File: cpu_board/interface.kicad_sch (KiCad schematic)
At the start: 10 parts, among them J5 Conn_01x06, J8 Conn_01x02

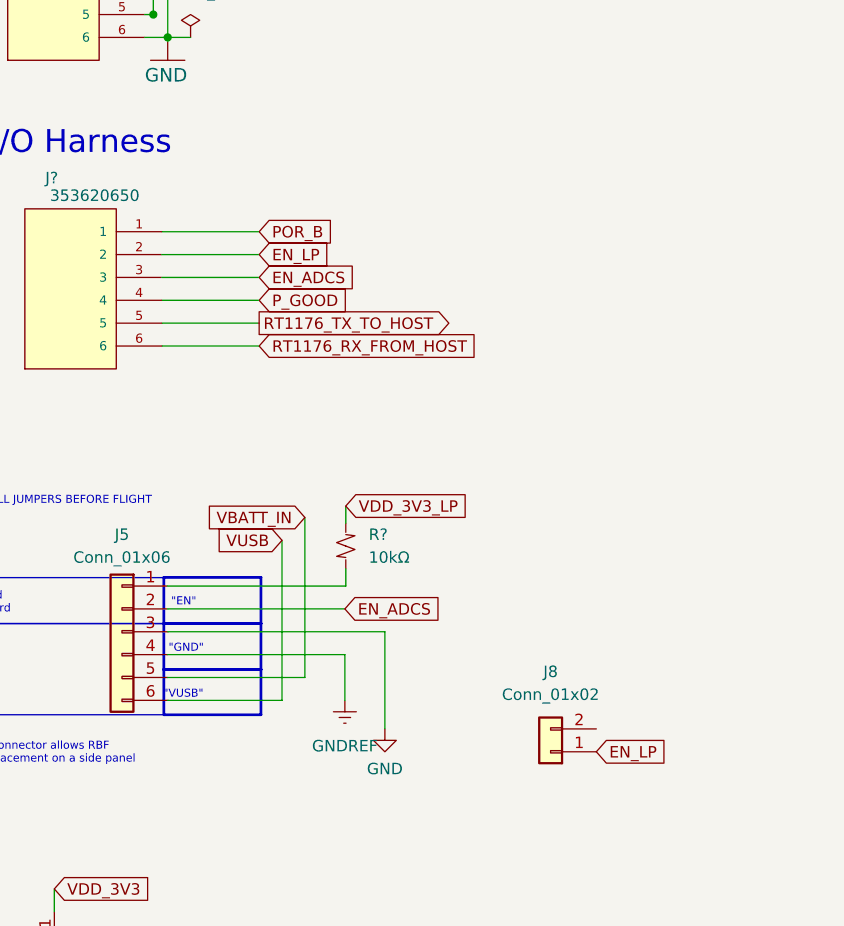
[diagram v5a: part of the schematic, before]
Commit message: move level shifter to top
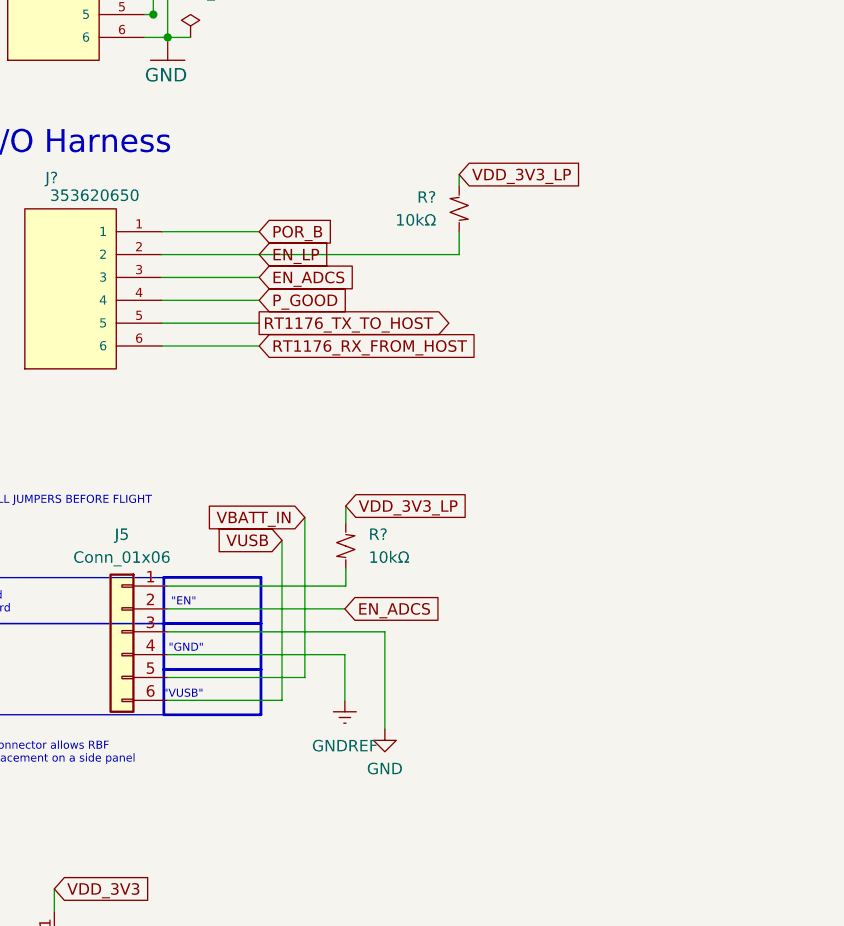
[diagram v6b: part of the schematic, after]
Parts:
- removed J8: Conn_01x02, symbol Connector_Generic:Conn_01x02
- added R?: 10kΩ, adcs:Perfect_0402, symbol Device:R_Small_US
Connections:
- net EN_LP: now also R?.2
- net VDD_3V3_LP: now also R?.1
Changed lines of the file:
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@@
   (junction (at 198.755 93.345) (diameter 0) (color 0 0 0 0)
   )
+  (wire (pts (xy 231.14 117.475) (xy 198.12 117.475))
+    (stroke (width 0) (type default))
+  )
   (wire (pts (xy 198.755 93.345) (xy 196.215 93.345))
     (stroke (width 0) (type default))
@@
     (stroke (width 0) (type default))
   )
+  (wire (pts (xy 231.14 114.935) (xy 231.14 117.475))
+    (stroke (width 0) (type default))
+  )
   (wire (pts (xy 198.12 125.095) (xy 208.915 125.095))
     (stroke (width 0) (type default))
   )
-  (wire (pts (xy 198.12 117.475) (xy 208.915 117.475))
-    (stroke (width 0) (type default))
-  )
   (wire (pts (xy 198.755 159.385) (xy 222.885 159.385))
     (stroke (width 0) (type default))
@@
   )
   (wire (pts (xy 197.1548 90.8304) (xy 197.1548 90.805))
+    (stroke (width 0) (type default))
+  )
+  (wire (pts (xy 231.14 108.585) (xy 231.14 109.855))
     (stroke (width 0) (type default))
   )
@@
   (text "Mounting Holes" (at 300.99 182.88 0)
     (effects (font (size 2.159 2.159)) (justify left bottom))
+  )
+  (global_label "VDD_3V3_LP" (shape input) (at 231.14 108.585 0) (fields_autoplaced)
+    (effects (font (size 1.27 1.27)) (justify left))
+    (property "Intersheetrefs" "${INTERSHEET_REFS}" (at 245.4947 108.585 0)
+      (effects (font (size 1.27 1.27)) (justify left) hide)
+    )
   )
   (global_label "VBATT_IN" (shape input) (at 198.755 80.645 0) (fields_autoplaced)
@@
     (property "Intersheetrefs" "${INTERSHEET_REFS}" (at 202.7245 146.685 0)
       (effects (font (size 1.27 1.27)) (justify right) hide)
-    )
-  )
-  (global_label "EN_LP" (shape input) (at 246.38 172.72 0) (fields_autoplaced)
-    (effects (font (size 1.27 1.27)) (justify left))
-    (property "Intersheetrefs" "${INTERSHEET_REFS}" (at 255.1104 172.72 0)
-      (effects (font (size 1.27 1.27)) (justify left) hide)
     )
   )
@@
         (path "/db20b18b-d25a-428e-8229-70a189e1de75/00000000-0000-0000-0000-00005cec60eb"
           (reference "J?") (unit 1)
-        )
-      )
-    )
-  )
-  (symbol (lib_id "Connector_Generic:Conn_01x02") (at 241.3 172.72 180) (unit 1)
-    (in_bom yes) (on_board yes) (dnp no) (fields_autoplaced)
-    (property "Reference" "J8" (at 241.3 163.83 0)
-      (effects (font (size 1.27 1.27)))
-    )
-    (property "Value" "Conn_01x02" (at 241.3 166.37 0)
-      (effects (font (size 1.27 1.27)))
-    )
-    (property "Footprint" "" (at 241.3 172.72 0)
-      (effects (font (size 1.27 1.27)) hide)
-    )
-    (property "Datasheet" "~" (at 241.3 172.72 0)
-      (effects (font (size 1.27 1.27)) hide)
-    )
-    (pin "1")
-    (pin "2")
-    (instances
-      (project "cpu_board"
-        (path "/c4fd7bdd-408e-44be-b66f-e6a18a0ca6e3/cea27ea3-b252-471b-8ae3-89651d2bf5e1"
-          (reference "J8") (unit 1)
         )
       )
@@
         )
       )
+    )
+  )
+  (symbol (lib_id "Device:R_Small_US") (at 231.14 112.395 0) (mirror y) (unit 1)
+    (in_bom yes) (on_board yes) (dnp no)
+    (property "Reference" "R?" (at 228.6 111.125 0)
+      (effects (font (size 1.27 1.27)) (justify left))
+    )
+    (property "Value" "10kΩ" (at 228.6 113.665 0)
+      (effects (font (size 1.27 1.27)) (justify left))
+    )
+    (property "Footprint" "adcs:Perfect_0402" (at 231.14 112.395 0)
+      (effects (font (size 1.27 1.27)) hide)
+    )
+    (property "Datasheet" "" (at 231.14 112.395 0)
+      (effects (font (size 1.27 1.27)) hide)
+    )
+    (property "JLCPCB P/N" "" (at 231.14 112.395 0)
+      (effects (font (size 1.27 1.27)) hide)
+    )
+    (property "JLCPCB P/N Proto" "" (at 231.14 112.395 0)
+      (effects (font (size 1.27 1.27)) hide)
+    )
+    (property "Footprint (for JLCPCB)" "0402" (at 231.14 112.395 0)
+      (effects (font (size 1.27 1.27)) hide)
+    )
+    (property "DigiKey Part Number" "" (at 231.14 112.395 0)
+      (effects (font (size 1.27 1.27)) hide)
+    )
+    (property "Tolerance" "" (at 231.14 112.395 0)
+      (effects (font (size 1.27 1.27)))
+    )
+    (property "Power Rating" "" (at 231.14 112.395 0)
+      (effects (font (size 1.27 1.27)))
+    )
+    (pin "1")
+    (pin "2")
+    (instances
+      (project "cpu_board"
+        (path "/c4fd7bdd-408e-44be-b66f-e6a18a0ca6e3/9cbcd73e-afcb-4ff3-8583-4372f7e826ca"
+          (reference "R?") (unit 1)
+        )
+        (path "/c4fd7bdd-408e-44be-b66f-e6a18a0ca6e3/41b8ad77-fc22-40ff-9aa2-f9a432177b3d"
+          (reference "R?") (unit 1)
+        )
+        (path "/c4fd7bdd-408e-44be-b66f-e6a18a0ca6e3/0a33bd80-4856-46ea-ab2b-780eb050e9ec"
+          (reference "R?") (unit 1)
+        )
+        (path "/c4fd7bdd-408e-44be-b66f-e6a18a0ca6e3/7dc61a70-8d21-4309-b5a7-f9382e73e709"
+          (reference "R?") (unit 1)
+        )
+        (path "/c4fd7bdd-408e-44be-b66f-e6a18a0ca6e3/7fac9943-67c1-4bb1-9a63-8a5404d1c1d4"
+          (reference "R?") (unit 1)
+        )
+        (path "/c4fd7bdd-408e-44be-b66f-e6a18a0ca6e3/cea27ea3-b252-471b-8ae3-89651d2bf5e1"
+          (reference "R4") (unit 1)
+        )
+      )

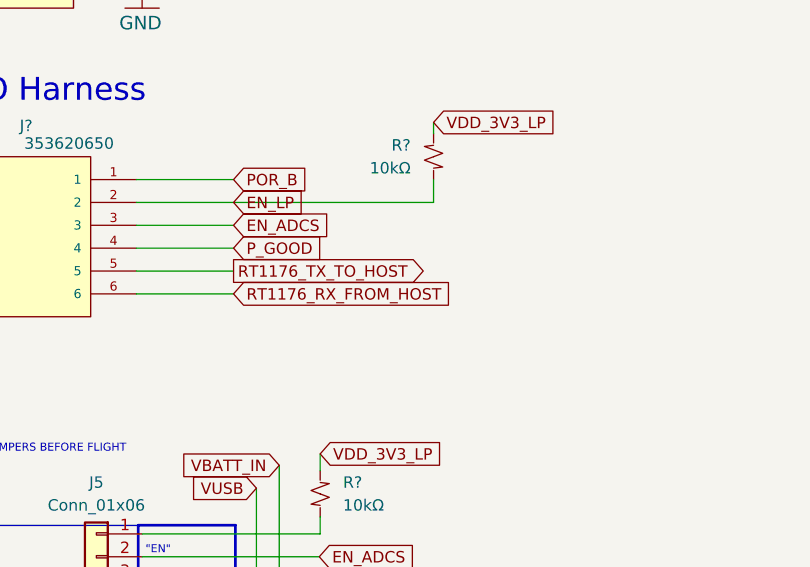
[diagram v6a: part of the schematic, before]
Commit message: clean up silkscreen
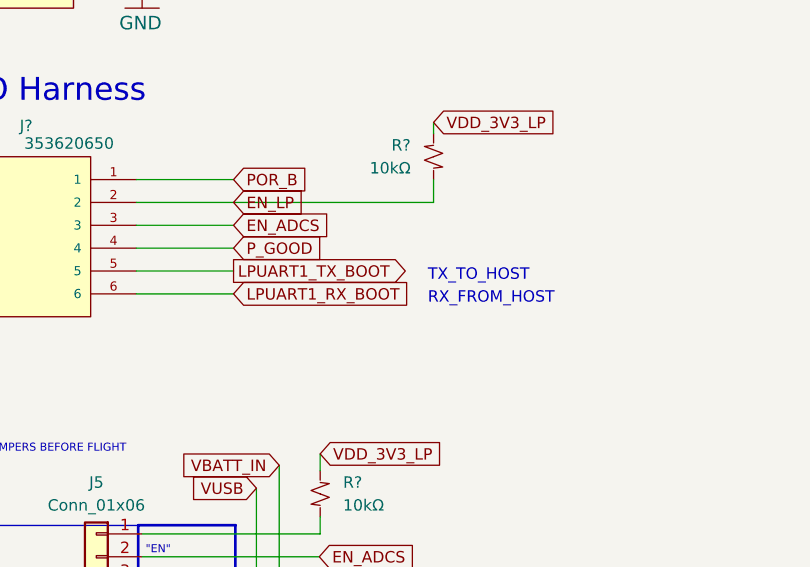
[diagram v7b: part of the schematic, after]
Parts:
- J5: DNI (none) -> DNI
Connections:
- net RT1176_RX_FROM_HOST renamed LPUART1_RX_BOOT
- net RT1176_TX_TO_HOST renamed LPUART1_TX_BOOT
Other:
- note added: "RX_FROM_HOST"
- note added: "TX_TO_HOST"
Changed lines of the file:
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@@
     (effects (font (size 0.889 0.889)) (justify right bottom))
+  )
+  (text "TX_TO_HOST" (at 230.505 126.365 0)
+    (effects (font (size 1.27 1.27)) (justify left bottom))
   )
   (text "Control and I/O Harness" (at 157.5308 106.6292 0)
     (effects (font (size 2.54 2.54)) (justify left bottom))
+  )
+  (text "RX_FROM_HOST" (at 230.505 128.905 0)
+    (effects (font (size 1.27 1.27)) (justify left bottom))
   )
   (text "\"VUSB\"" (at 198.2724 166.9542 0)
@@
     )
   )
-  (global_label "RT1176_RX_FROM_HOST" (shape input) (at 208.915 127.635 0) (fields_autoplaced)
-    (effects (font (size 1.27 1.27)) (justify left))
-    (property "Intersheetrefs" "${INTERSHEET_REFS}" (at 234.3367 127.635 0)
-      (effects (font (size 1.27 1.27)) (justify left) hide)
-    )
-  )
   (global_label "VDD_3V3" (shape input) (at 186.1566 187.96 0) (fields_autoplaced)
     (effects (font (size 1.27 1.27)) (justify left))
@@
     (effects (font (size 1.27 1.27)) (justify left))
     (property "Intersheetrefs" "${INTERSHEET_REFS}" (at 209.9456 205.74 0)
+      (effects (font (size 1.27 1.27)) (justify left) hide)
+    )
+  )
+  (global_label "LPUART1_TX_BOOT" (shape output) (at 208.915 125.095 0) (fields_autoplaced)
+    (effects (font (size 1.27 1.27)) (justify left))
+    (property "Intersheetrefs" "${INTERSHEET_REFS}" (at 229.0754 125.095 0)
       (effects (font (size 1.27 1.27)) (justify left) hide)
     )
@@
     )
   )
+  (global_label "LPUART1_RX_BOOT" (shape input) (at 208.915 127.635 0) (fields_autoplaced)
+    (effects (font (size 1.27 1.27)) (justify left))
+    (property "Intersheetrefs" "${INTERSHEET_REFS}" (at 229.3778 127.635 0)
+      (effects (font (size 1.27 1.27)) (justify left) hide)
+    )
+  )
   (global_label "SWD_CLK" (shape input) (at 198.8566 203.2 0) (fields_autoplaced)
     (effects (font (size 1.27 1.27)) (justify left))
     (property "Intersheetrefs" "${INTERSHEET_REFS}" (at 210.3084 203.2 0)
-      (effects (font (size 1.27 1.27)) (justify left) hide)
-    )
-  )
-  (global_label "RT1176_TX_TO_HOST" (shape output) (at 208.915 125.095 0) (fields_autoplaced)
-    (effects (font (size 1.27 1.27)) (justify left))
-    (property "Intersheetrefs" "${INTERSHEET_REFS}" (at 231.1919 125.095 0)
       (effects (font (size 1.27 1.27)) (justify left) hide)
     )
@@
       (effects (font (size 1.27 1.27)) hide)
     )
-    (property "Datasheet" "~" (at 193.675 159.385 0)
+    (property "Datasheet" "" (at 193.675 159.385 0)
       (effects (font (size 1.27 1.27)) hide)
     )
@@
       (effects (font (size 1.27 1.27)))
     )
-    (pin "1")
+    (property "DNI" "DNI" (at 193.675 159.385 0)
+      (effects (font (size 1.27 1.27)) hide)
+    )
+    (pin "1")

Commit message: soldermander 1.0 ready for review
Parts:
- H1: now left out of the parts list
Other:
- note added: "7-10V input"
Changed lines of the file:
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@@
     (effects (font (size 0.889 0.889)) (justify right bottom))
+  )
+  (text "7-10V\ninput" (at 156.845 90.17 0)
+    (effects (font (size 2.54 2.54) (thickness 0.508) bold) (justify left bottom))
   )
   (text "TX_TO_HOST" (at 230.505 126.365 0)
@@
   )
   (symbol (lib_id "Mechanical:MountingHole_Pad") (at 313.69 187.96 90) (unit 1)
-    (in_bom yes) (on_board yes) (dnp no)
+    (in_bom no) (on_board yes) (dnp no)
     (property "Reference" "H1" (at 307.34 187.96 90)
       (effects (font (size 1.27 1.27)))
@@
     )
     (property "DNI" "DNI" (at 313.69 195.58 0)
+      (effects (font (size 1.27 1.27)) hide)
+    )
+    (property "DigiKey Part Number" "" (at 313.69 195.58 0)
+      (effects (font (size 1.27 1.27)) hide)
+    )
+    (property "Tolerance" "" (at 313.69 195.58 0)
+      (effects (font (size 1.27 1.27)))
+    )
+    (property "Power Rating" "" (at 313.69 195.58 0)
+      (effects (font (size 1.27 1.27)))
+    )
+    (property "Sim.Enable" "0" (at 313.69 195.58 0)
       (effects (font (size 1.27 1.27)) hide)
     )
@@
       (effects (font (size 1.27 1.27)) hide)
     )
+    (property "DigiKey Part Number" "" (at 313.69 199.39 0)
+      (effects (font (size 1.27 1.27)) hide)
+    )
+    (property "Tolerance" "" (at 313.69 199.39 0)
+      (effects (font (size 1.27 1.27)))
+    )
+    (property "Power Rating" "" (at 313.69 199.39 0)
+      (effects (font (size 1.27 1.27)))
+    )
+    (property "Sim.Enable" "0" (at 313.69 199.39 0)
+      (effects (font (size 1.27 1.27)) hide)
+    )
     (pin "1")
     (instances
@@
       (effects (font (size 1.27 1.27)) hide)
     )
+    (property "DigiKey Part Number" "" (at 313.69 191.77 0)
+      (effects (font (size 1.27 1.27)) hide)
+    )
+    (property "Tolerance" "" (at 313.69 191.77 0)
+      (effects (font (size 1.27 1.27)))
+    )
+    (property "Power Rating" "" (at 313.69 191.77 0)
+      (effects (font (size 1.27 1.27)))
+    )
+    (property "Sim.Enable" "0" (at 313.69 191.77 0)
+      (effects (font (size 1.27 1.27)) hide)
+    )
